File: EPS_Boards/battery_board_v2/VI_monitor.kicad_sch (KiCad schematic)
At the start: 4 parts

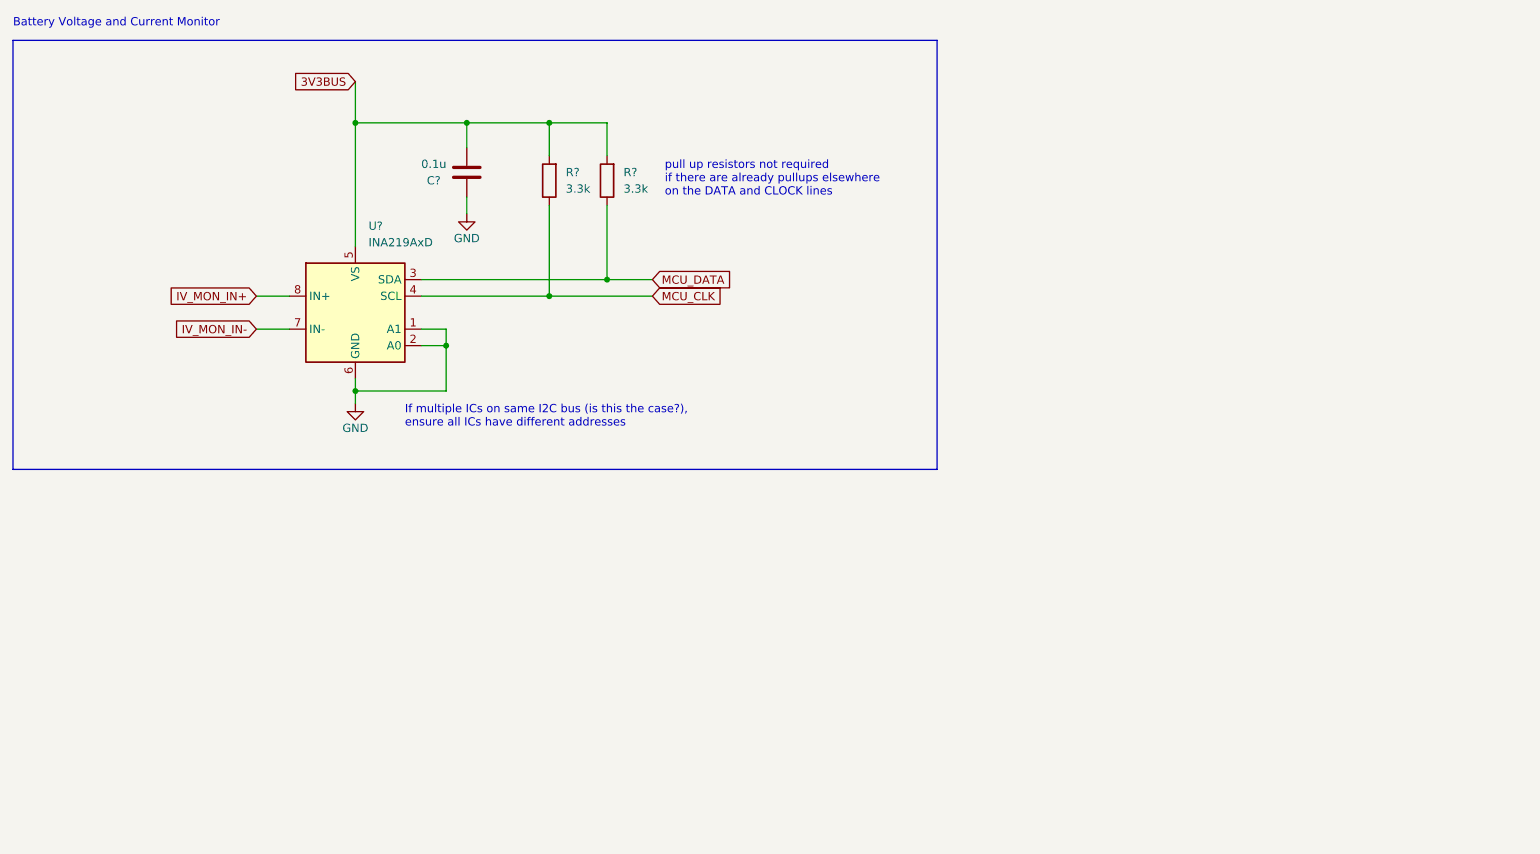
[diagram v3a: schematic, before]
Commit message: eps: battery board: finializing schematic
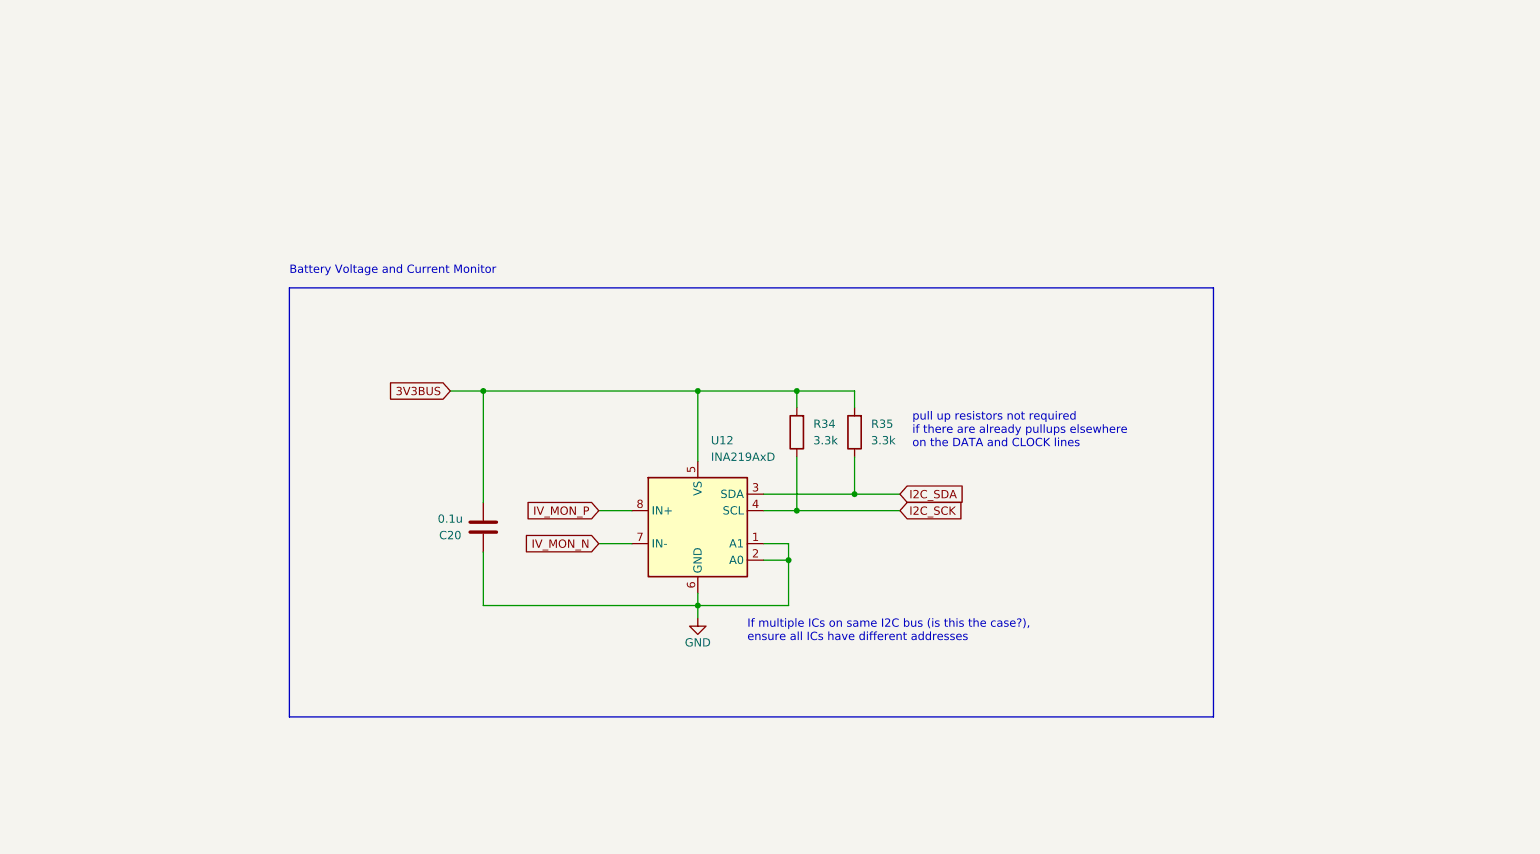
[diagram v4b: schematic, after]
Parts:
- gave numbers to parts that had none: 4
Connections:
- net IV_MON_IN+ renamed IV_MON_P
- net IV_MON_IN- renamed IV_MON_N
- net MCU_CLK renamed I2C_SCK
- net MCU_DATA renamed I2C_SDA
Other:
- moved on the sheet: C20, R34, R35, U12

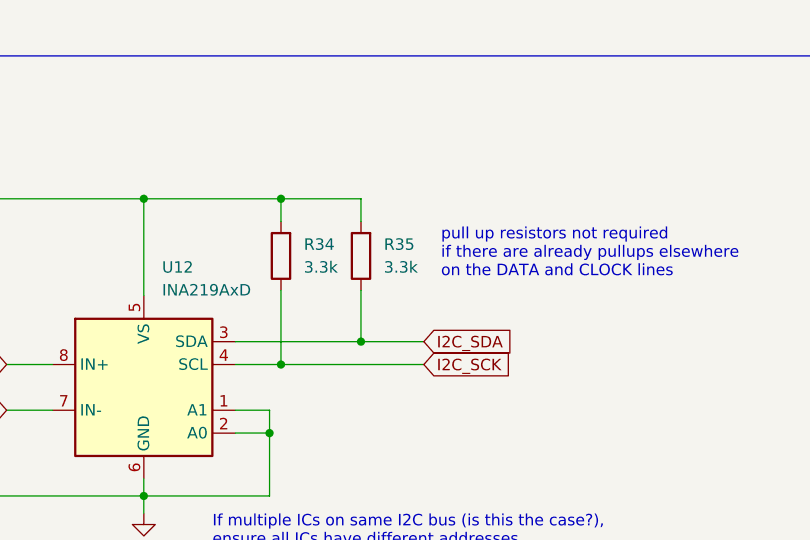
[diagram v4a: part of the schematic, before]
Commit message: eps: battery board: updated board layout
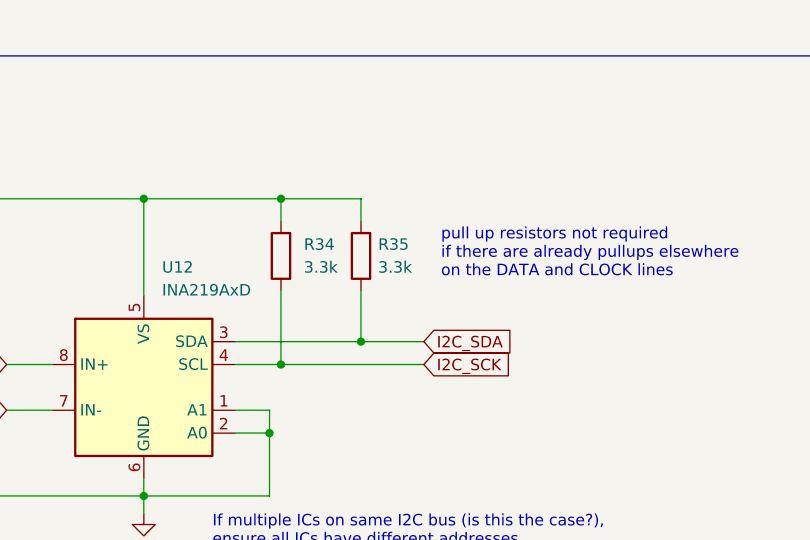
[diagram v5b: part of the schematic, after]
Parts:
- C20: footprint (none) -> Capacitor_SMD:C_0402_1005Metric
- R34, R35: footprint (none) -> Resistor_SMD:R_0402_1005Metric
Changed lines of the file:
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@@
   (symbol (lib_id "Device:R") (at 151.765 87.63 180) (unit 1)
     (in_bom yes) (on_board yes) (fields_autoplaced)
-    (property "Reference" "R35" (id 0) (at 154.305 86.3599 0)
+    (property "Reference" "R35" (id 0) (at 153.67 86.3599 0)
       (effects (font (size 1.27 1.27)) (justify right))
     )
-    (property "Value" "3.3k" (id 1) (at 154.305 88.8999 0)
+    (property "Value" "3.3k" (id 1) (at 153.67 88.8999 0)
       (effects (font (size 1.27 1.27)) (justify right))
     )
-    (property "Footprint" "" (id 2) (at 153.543 87.63 90)
+    (property "Footprint" "Resistor_SMD:R_0402_1005Metric" (id 2) (at 153.543 87.63 90)
       (effects (font (size 1.27 1.27)) hide)
     )
@@
       (effects (font (size 1.27 1.27)) (justify right))
     )
-    (property "Footprint" "" (id 2) (at 144.653 87.63 90)
+    (property "Footprint" "Resistor_SMD:R_0402_1005Metric" (id 2) (at 144.653 87.63 90)
       (effects (font (size 1.27 1.27)) hide)
     )
@@
     (property "Reference" "C20" (id 0) (at 89.535 103.505 0))
     (property "Value" "0.1u" (id 1) (at 89.535 100.965 0))
-    (property "Footprint" "" (id 2) (at 93.6498 98.425 0)
+    (property "Footprint" "Capacitor_SMD:C_0402_1005Metric" (id 2) (at 93.6498 98.425 0)
       (effects (font (size 1.27 1.27)) hide)
     )

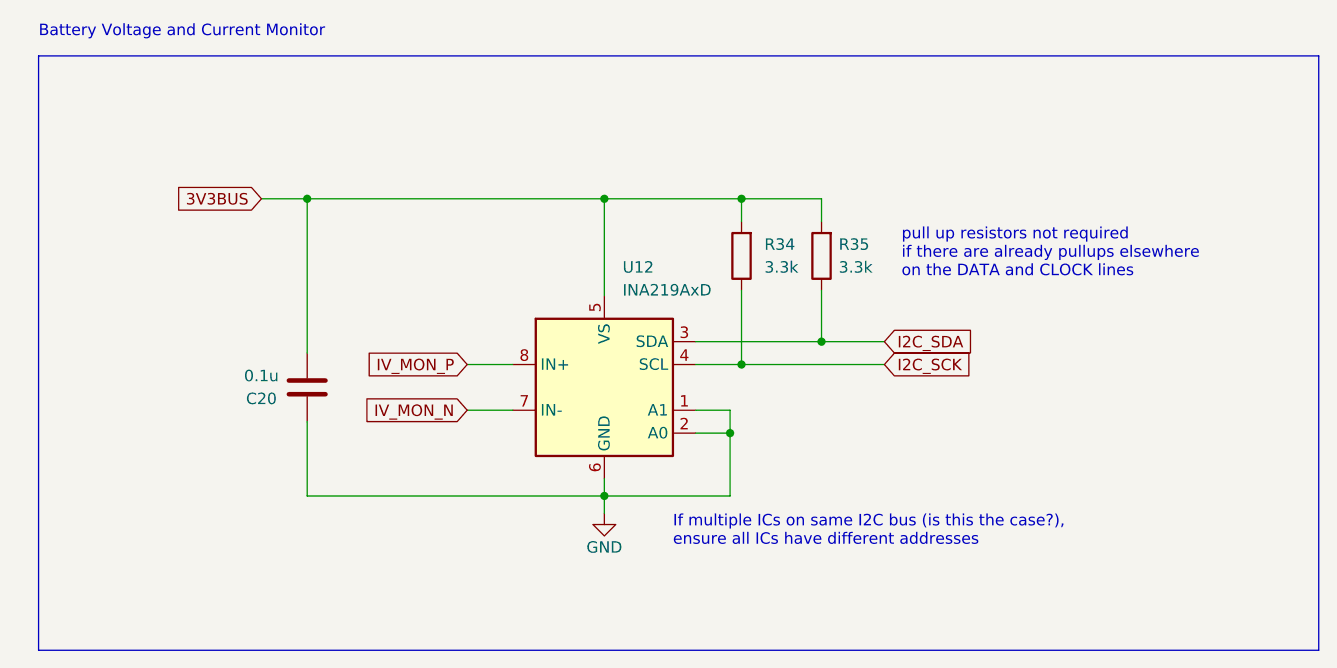
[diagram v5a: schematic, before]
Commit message: eps: battery board: added EDS protection
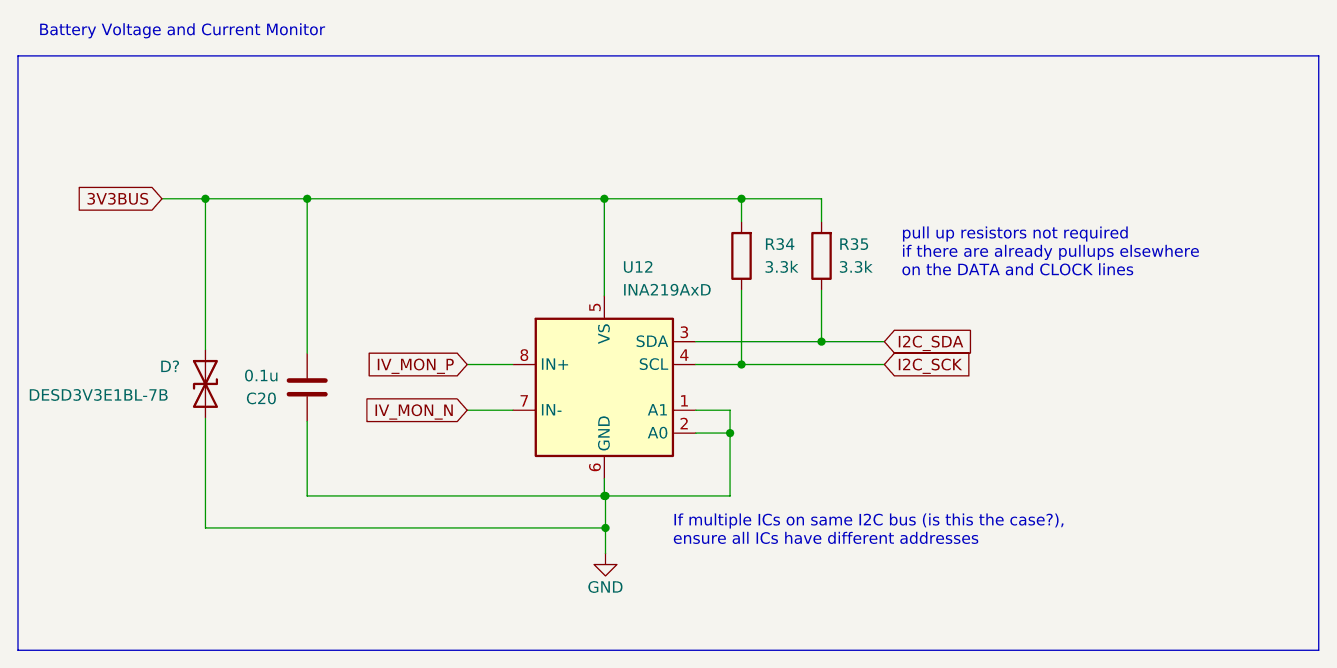
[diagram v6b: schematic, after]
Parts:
- added D?: DESD3V3E1BL-7B, Resistor_SMD:R_0201_0603Metric, symbol Device:D_TVS
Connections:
- net 3V3BUS: now also D?.1 (A1)
- net GND: now also D?.2 (A2)
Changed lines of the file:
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@@
   (junction (at 141.605 107.315) (diameter 0) (color 0 0 0 0)
   )
+  (junction (at 127.762 117.856) (diameter 0) (color 0 0 0 0)
+  )
+  (junction (at 83.312 81.28) (diameter 0) (color 0 0 0 0)
+  )
   (junction (at 94.615 81.28) (diameter 0) (color 0 0 0 0)
   )
   (junction (at 142.875 99.695) (diameter 0) (color 0 0 0 0)
   )
+  (junction (at 127.762 114.3) (diameter 0) (color 0 0 0 0)
+  )
   (junction (at 142.875 81.28) (diameter 0) (color 0 0 0 0)
   )
@@
   (junction (at 151.765 97.155) (diameter 0) (color 0 0 0 0)
   )
+  (wire (pts (xy 127.762 117.856) (xy 127.762 120.65))
+    (stroke (width 0) (type default) (color 0 0 0 0))
+  )
   (wire (pts (xy 117.475 99.695) (xy 112.395 99.695))
     (stroke (width 0) (type default) (color 0 0 0 0))
   )
-  (wire (pts (xy 89.535 81.28) (xy 94.615 81.28))
+  (wire (pts (xy 78.486 81.28) (xy 83.312 81.28))
     (stroke (width 0) (type default) (color 0 0 0 0))
   )
@@
     (stroke (width 0) (type default) (color 0 0 0 0))
   )
-  (polyline (pts (xy 64.77 131.445) (xy 64.77 65.405))
+  (polyline (pts (xy 62.484 131.445) (xy 62.484 65.405))
     (stroke (width 0) (type default) (color 0 0 0 0))
   )
@@
     (stroke (width 0) (type default) (color 0 0 0 0))
   )
+  (wire (pts (xy 83.312 105.664) (xy 83.312 117.856))
+    (stroke (width 0) (type default) (color 0 0 0 0))
+  )
+  (wire (pts (xy 83.312 81.28) (xy 94.615 81.28))
+    (stroke (width 0) (type default) (color 0 0 0 0))
+  )
   (wire (pts (xy 142.875 91.44) (xy 142.875 99.695))
     (stroke (width 0) (type default) (color 0 0 0 0))
   )
-  (polyline (pts (xy 207.01 131.445) (xy 64.77 131.445))
+  (polyline (pts (xy 207.01 131.445) (xy 62.484 131.445))
     (stroke (width 0) (type default) (color 0 0 0 0))
   )
@@
     (stroke (width 0) (type default) (color 0 0 0 0))
   )
+  (wire (pts (xy 83.312 117.856) (xy 127.762 117.856))
+    (stroke (width 0) (type default) (color 0 0 0 0))
+  )
+  (wire (pts (xy 127.762 114.3) (xy 127.635 114.3))
+    (stroke (width 0) (type default) (color 0 0 0 0))
+  )
   (wire (pts (xy 151.765 97.155) (xy 158.75 97.155))
     (stroke (width 0) (type default) (color 0 0 0 0))
   )
+  (wire (pts (xy 127.762 114.3) (xy 127.762 117.856))
+    (stroke (width 0) (type default) (color 0 0 0 0))
+  )
   (wire (pts (xy 142.875 99.695) (xy 158.75 99.695))
     (stroke (width 0) (type default) (color 0 0 0 0))
   )
-  (polyline (pts (xy 64.77 65.405) (xy 207.01 65.405))
+  (polyline (pts (xy 62.484 65.405) (xy 207.01 65.405))
     (stroke (width 0) (type default) (color 0 0 0 0))
   )
@@
     (stroke (width 0) (type default) (color 0 0 0 0))
   )
+  (wire (pts (xy 83.312 81.28) (xy 83.312 98.044))
+    (stroke (width 0) (type default) (color 0 0 0 0))
+  )
   (wire (pts (xy 127.635 112.395) (xy 127.635 114.3))
     (stroke (width 0) (type default) (color 0 0 0 0))
   )
-  (wire (pts (xy 127.635 114.3) (xy 127.635 116.205))
-    (stroke (width 0) (type default) (color 0 0 0 0))
-  )
   (wire (pts (xy 94.615 106.045) (xy 94.615 114.3))
     (stroke (width 0) (type default) (color 0 0 0 0))
@@
     (stroke (width 0) (type default) (color 0 0 0 0))
   )
-  (wire (pts (xy 141.605 114.3) (xy 127.635 114.3))
+  (wire (pts (xy 141.605 114.3) (xy 127.762 114.3))
     (stroke (width 0) (type default) (color 0 0 0 0))
   )
@@
     )
   )
-  (global_label "3V3BUS" (shape input) (at 89.535 81.28 180) (fields_autoplaced)
+  (global_label "3V3BUS" (shape input) (at 78.486 81.28 180) (fields_autoplaced)
     (effects (font (size 1.27 1.27)) (justify right))
-    (property "Intersheet References" "${INTERSHEET_REFS}" (id 0) (at 79.8932 81.2006 0)
+    (property "Intersheet References" "${INTERSHEET_REFS}" (id 0) (at 68.8442 81.2006 0)
       (effects (font (size 1.27 1.27)) (justify right) hide)
     )
@@
     (pin "2")
   )
+  (symbol (lib_id "Device:D_TVS") (at 83.312 101.854 90) (mirror x) (unit 1)
+    (in_bom yes) (on_board yes)
+    (property "Reference" "D?" (id 0) (at 78.232 99.949 90)
+      (effects (font (size 1.27 1.27)) (justify right))
+    )
+    (property "Value" "DESD3V3E1BL-7B" (id 1) (at 63.627 103.124 90)
+      (effects (font (size 1.27 1.27)) (justify right))
+    )
+    (property "Footprint" "Resistor_SMD:R_0201_0603Metric" (id 2) (at 83.312 101.854 0)
+      (effects (font (size 1.27 1.27)) hide)
+    )
+    (property "Datasheet" "https://www.diodes.com/assets/Datasheets/DESD3V3E1BL.pdf" (id 3) (at 83.312 101.854 0)
+      (effects (font (size 1.27 1.27)) hide)
+    )
+    (pin "1")
+    (pin "2")
+  )
   (symbol (lib_id "Device:R") (at 142.875 87.63 180) (unit 1)
     (in_bom yes) (on_board yes) (fields_autoplaced)
@@
     (pin "2")
   )
-  (symbol (lib_id "power:GND") (at 127.635 116.205 0) (unit 1)
+  (symbol (lib_id "power:GND") (at 127.762 120.65 0) (unit 1)
     (in_bom yes) (on_board yes)
-    (property "Reference" "#PWR0117" (id 0) (at 127.635 122.555 0)
-      (effects (font (size 1.27 1.27)) hide)
-    )
-    (property "Value" "GND" (id 1) (at 127.635 120.015 0))
-    (property "Footprint" "" (id 2) (at 127.635 116.205 0)
-      (effects (font (size 1.27 1.27)) hide)
-    )
-    (property "Datasheet" "" (id 3) (at 127.635 116.205 0)
-      (effects (font (size 1.27 1.27)) hide)
-    )
+    (property "Reference" "#PWR0117" (id 0) (at 127.762 127 0)
+      (effects (font (size 1.27 1.27)) hide)
+    )
+    (property "Value" "GND" (id 1) (at 127.762 124.46 0))
+    (property "Footprint" "" (id 2) (at 127.762 120.65 0)
+      (effects (font (size 1.27 1.27)) hide)
+    )
+    (property "Datasheet" "" (id 3) (at 127.762 120.65 0)
+      (effects (font (size 1.27 1.27)) hide)
+    )

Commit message: eps: battery board: progress on pcb layout
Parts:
- gave numbers to parts that had none: 1
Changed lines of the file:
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@@
   (symbol (lib_id "Device:D_TVS") (at 83.312 101.854 90) (mirror x) (unit 1)
     (in_bom yes) (on_board yes)
-    (property "Reference" "D?" (id 0) (at 78.232 99.949 90)
+    (property "Reference" "D4" (id 0) (at 78.232 99.949 90)
       (effects (font (size 1.27 1.27)) (justify right))
     )

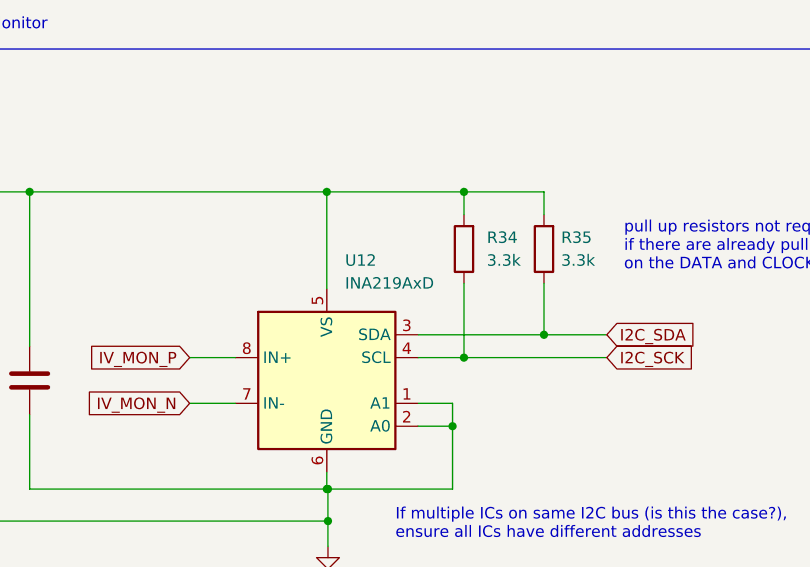
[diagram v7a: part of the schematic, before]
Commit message: eps: battery board: updated board layout
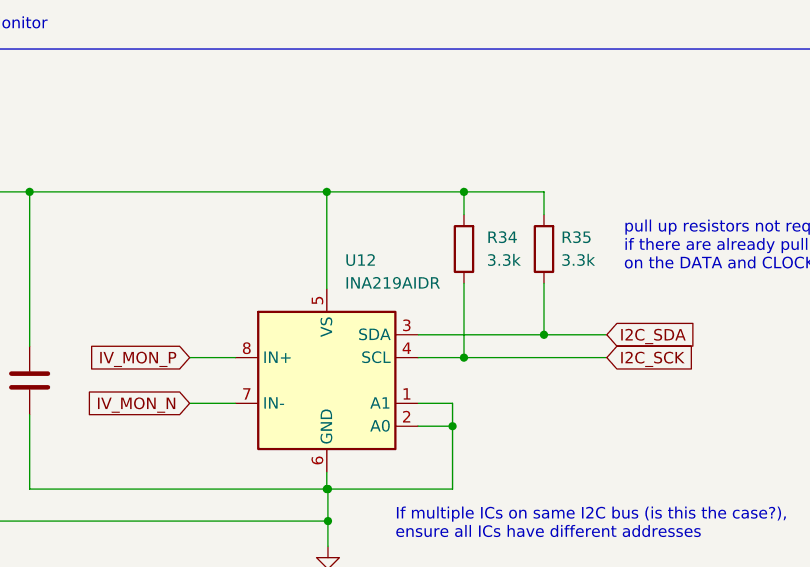
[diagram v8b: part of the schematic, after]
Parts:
- U12: value INA219AxD -> INA219AIDR
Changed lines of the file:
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@@
       (effects (font (size 1.27 1.27)) (justify left))
     )
-    (property "Value" "INA219AxD" (id 1) (at 129.6544 91.44 0)
+    (property "Value" "INA219AIDR" (id 1) (at 129.6544 91.44 0)
       (effects (font (size 1.27 1.27)) (justify left))
     )
